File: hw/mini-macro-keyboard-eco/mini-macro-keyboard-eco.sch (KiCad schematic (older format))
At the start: 32 parts, among them J0 USB, J1 DEBUG_SWD, SW1 SW_Cherry_MX_1.00u_PCB, SW2 SW_Cherry_MX_1.00u_PCB, SW3 SW_Cherry_MX_1.00u_PCB, SW5 LAYOUT, SW6 BACKLIGHT, U1 USBLC6-2SC6, U2 XC6206P322MR, U3 STM32F070F6P6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

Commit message: feat(hw): add rooting
Signed-off-by: Ivan Kovalenko <s1ckretbox@gmail.com>
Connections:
- net LED_1: now also U3.9 (PA3); no longer U3.6 (PA0)
- net LED_3: now also U3.6 (PA0); no longer U3.9 (PA3)
- net SW_1: now also U3.13 (PA7); no longer U3.11 (PA5)
- net SW_3: now also U3.11 (PA5); no longer U3.13 (PA7)
- net USB_CONN_D+: now also U1.3 (I/O2); no longer U1.1 (I/O1)
- net USB_CONN_D-: now also U1.1 (I/O1); no longer U1.3 (I/O2)
- net USB_D+: now also U1.4 (I/O2); no longer U1.6 (I/O1)
- net USB_D-: now also U1.6 (I/O1); no longer U1.4 (I/O2)
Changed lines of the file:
@@
 Text GLabel 4350 3000 2    50   Input ~ 0
 USB_D-
-Text GLabel 4350 2500 2    50   Input ~ 0
+Text GLabel 4350 2200 2    50   Input ~ 0
 LED_3
 Text GLabel 4350 2300 2    50   Input ~ 0
 LED_2
-Text GLabel 4350 2200 2    50   Input ~ 0
+Text GLabel 4350 2500 2    50   Input ~ 0
 LED_1
-Text GLabel 4350 2700 2    50   Input ~ 0
+Text GLabel 4350 2900 2    50   Input ~ 0
 SW_1
 Text GLabel 4350 2800 2    50   Input ~ 0
 SW_2
-Text GLabel 4350 2900 2    50   Input ~ 0
+Text GLabel 4350 2700 2    50   Input ~ 0
 SW_3
 Text GLabel 3050 3100 0    50   Input ~ 0
@@
 Text GLabel 1650 4950 2    50   Input ~ 0
 USB_CONN_D-
-Text GLabel 3200 4900 0    50   Input ~ 0
+Text GLabel 4000 4900 2    50   Input ~ 0
 USB_CONN_D+
 $Comp
@@
 	1    0    0    -1
 $EndComp
+Text GLabel 4000 4700 2    50   Input ~ 0
+USB_D+
+Text GLabel 3200 4900 0    50   Input ~ 0
+USB_CONN_D-
 Text GLabel 3200 4700 0    50   Input ~ 0
-USB_D+
-Text GLabel 4000 4900 2    50   Input ~ 0
-USB_CONN_D-
-Text GLabel 4000 4700 2    50   Input ~ 0
 USB_D-
 Text GLabel 7650 900  0    50   Input ~ 0

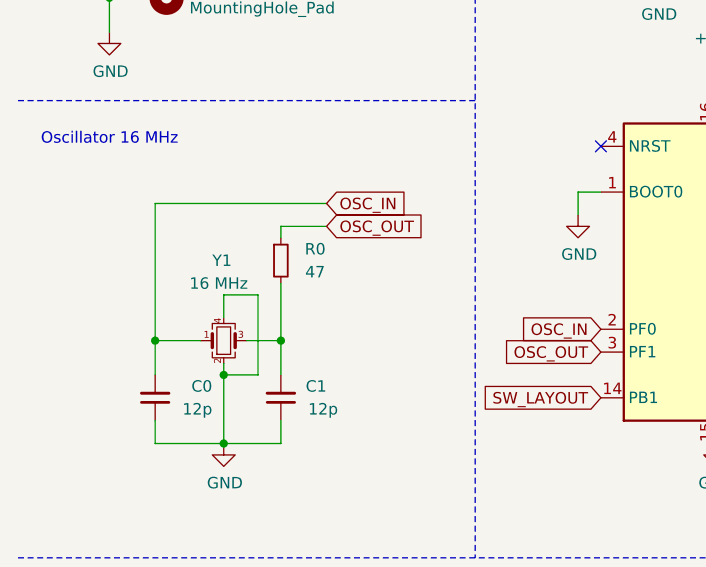
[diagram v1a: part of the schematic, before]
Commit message: fix(hw, #3): remove R0 resistor
Signed-off-by: Ivan Kovalenko <s1ckretbox@gmail.com>
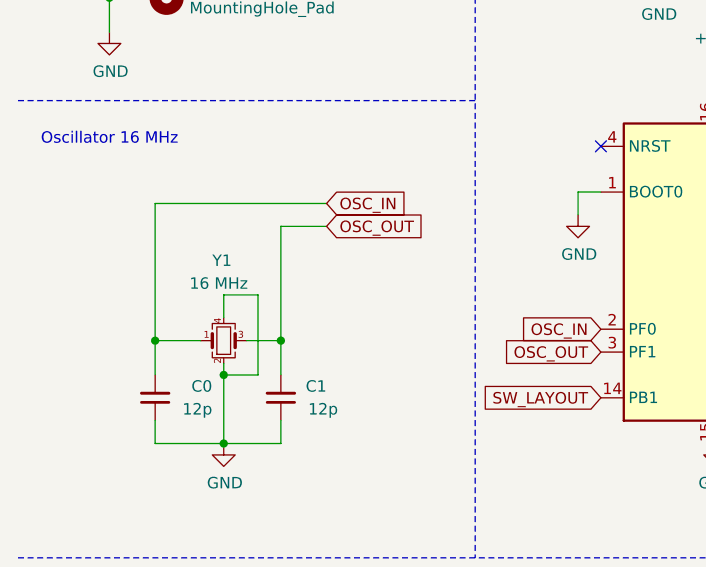
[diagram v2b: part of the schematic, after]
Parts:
- removed R0: 47, Resistor_SMD:R_0402_1005Metric, symbol mini-macro-keyboard-eco-rescue:R_Small-Device
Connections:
- net OSC_OUT: now also C1.2, Y1.3
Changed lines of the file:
@@
 	-1   0    0    1
-$EndComp
-$Comp
-L mini-macro-keyboard-eco-rescue:R_Small-Device R0
-U 1 1 60011E97
-P 1650 2700
-F 0 "R0" H 1800 2750 50  0000 C CNN
-F 1 "47" H 1800 2650 50  0000 C CNN
-F 2 "Resistor_SMD:R_0402_1005Metric" H 1650 2700 50  0001 C CNN
-F 3 "~" H 1650 2700 50  0001 C CNN
-	1    1650 2700
-	1    0    0    -1
 $EndComp
 Text GLabel 1850 2450 2    50   Input ~ 0
@@
 Wire Wire Line
 	1400 3200 1400 3500
-Wire Wire Line
-	1650 2800 1650 3050
 Connection ~ 1650 3050
 Connection ~ 1100 3050
 Wire Wire Line
 	1850 2550 1650 2550
-Wire Wire Line
-	1650 2550 1650 2600
 Wire Notes Line
 	7000 500  7000 2000
@@
 Wire Wire Line
 	900  1050 900  1300
+Wire Wire Line
+	1650 2550 1650 3050
 $EndSCHEMATC

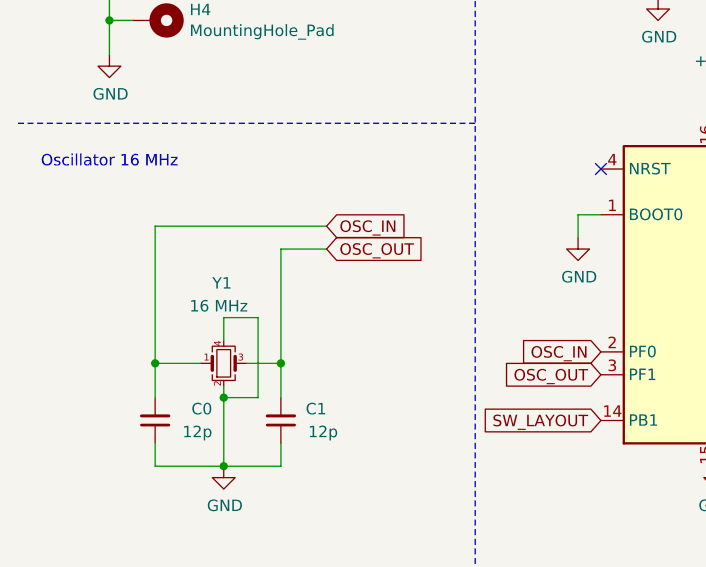
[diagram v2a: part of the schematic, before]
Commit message: feat(hw): add jlcpcb parts number
Signed-off-by: Ivan Kovalenko <s1ckretbox@gmail.com>
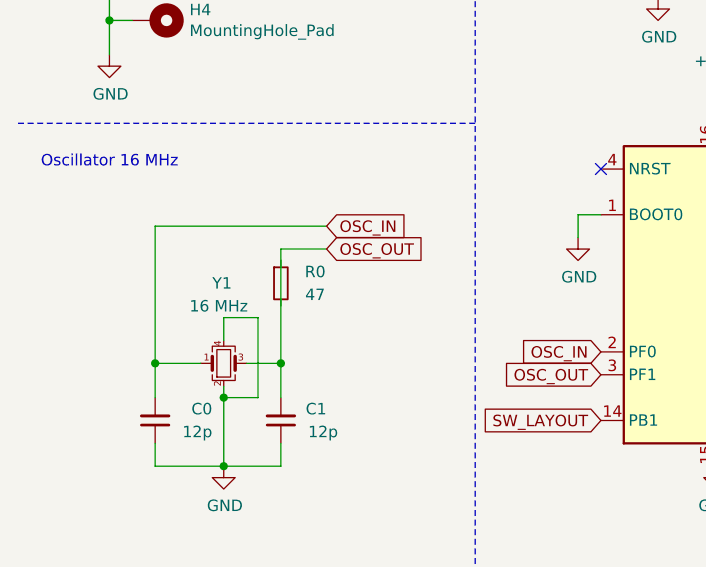
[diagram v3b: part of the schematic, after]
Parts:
- added R0: 47, Resistor_SMD:R_0402_1005Metric, symbol mini-macro-keyboard-eco-rescue:R_Small-Device
- C0, C1: LCSC Part # (none) -> C1547
- C2, C3, C7: LCSC Part # (none) -> C1525
- C4: LCSC Part # (none) -> C19666
- C5, C6: LCSC Part # (none) -> C52923
- D1, D2, D3: LCSC Part # (none) -> C72041
- R1, R2, R3: LCSC Part # (none) -> C23138
- R5, R6: LCSC Part # (none) -> C25744
- U1: LCSC Part # (none) -> C7519
- U2: LCSC Part # (none) -> C5446
- U3: LCSC Part # (none) -> C86951
- Y1: LCSC Part # (none) -> C13738
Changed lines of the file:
@@
 F 2 "Capacitor_SMD:C_0402_1005Metric" H 3300 1200 50  0001 C CNN
 F 3 "~" H 3300 1200 50  0001 C CNN
+F 4 "C1525" H 3300 1200 50  0001 C CNN "LCSC Part #"
 	1    3300 1200
 	1    0    0    -1
@@
 F 2 "Capacitor_SMD:C_0402_1005Metric" H 3600 1200 50  0001 C CNN
 F 3 "~" H 3600 1200 50  0001 C CNN
+F 4 "C1525" H 3600 1200 50  0001 C CNN "LCSC Part #"
 	1    3600 1200
 	1    0    0    -1
@@
 F 2 "Capacitor_SMD:C_0402_1005Metric" H 3950 1200 50  0001 C CNN
 F 3 "~" H 3950 1200 50  0001 C CNN
+F 4 "C19666" H 3950 1200 50  0001 C CNN "LCSC Part #"
 	1    3950 1200
 	1    0    0    -1
@@
 F 2 "Capacitor_SMD:C_0402_1005Metric" H 1100 3300 50  0001 C CNN
 F 3 "~" H 1100 3300 50  0001 C CNN
+F 4 "C1547" H 1100 3300 50  0001 C CNN "LCSC Part #"
 	1    1100 3300
 	-1   0    0    1
+$EndComp
+$Comp
+L mini-macro-keyboard-eco-rescue:R_Small-Device R0
+U 1 1 60011E97
+P 1650 2700
+F 0 "R0" H 1800 2750 50  0000 C CNN
+F 1 "47" H 1800 2650 50  0000 C CNN
+F 2 "Resistor_SMD:R_0402_1005Metric" H 1650 2700 50  0001 C CNN
+F 3 "~" H 1650 2700 50  0001 C CNN
+F 4 "C25792" H 1650 2700 50  0001 C CNN "LCSC Part #"
+	1    1650 2700
+	1    0    0    -1
 $EndComp
 Text GLabel 1850 2450 2    50   Input ~ 0
@@
 F 2 "Package_TO_SOT_SMD:SOT-23-6" H 3600 4300 50  0001 C CNN
 F 3 "https://www.st.com/resource/en/datasheet/usblc6-2.pdf" H 3800 5150 50  0001 C CNN
+F 4 "C7519" H 3600 4800 50  0001 C CNN "LCSC Part #"
 	1    3600 4800
 	1    0    0    -1
@@
 F 2 "LED_SMD:LED_0603_1608Metric" V 7900 900 50  0001 C CNN
 F 3 "~" V 7900 900 50  0001 C CNN
+F 4 "C72041" H 7900 900 50  0001 C CNN "LCSC Part #"
 	1    7900 900
 	-1   0    0    1
@@
 F 2 "Resistor_SMD:R_0603_1608Metric" H 8250 900 50  0001 C CNN
 F 3 "~" H 8250 900 50  0001 C CNN
+F 4 "C23138" H 8250 900 50  0001 C CNN "LCSC Part #"
 	1    8250 900
 	0    -1   -1   0
@@
 F 2 "LED_SMD:LED_0603_1608Metric" V 7900 1250 50  0001 C CNN
 F 3 "~" V 7900 1250 50  0001 C CNN
+F 4 "C72041" H 7900 1250 50  0001 C CNN "LCSC Part #"
 	1    7900 1250
 	-1   0    0    1
@@
 F 2 "Resistor_SMD:R_0603_1608Metric" H 8250 1250 50  0001 C CNN
 F 3 "~" H 8250 1250 50  0001 C CNN
+F 4 "C23138" H 8250 1250 50  0001 C CNN "LCSC Part #"
 	1    8250 1250
 	0    -1   -1   0
@@
 F 2 "LED_SMD:LED_0603_1608Metric" V 7900 1600 50  0001 C CNN
 F 3 "~" V 7900 1600 50  0001 C CNN
+F 4 "C72041" H 7900 1600 50  0001 C CNN "LCSC Part #"
 	1    7900 1600
 	-1   0    0    1
@@
 F 2 "Resistor_SMD:R_0603_1608Metric" H 8250 1600 50  0001 C CNN
 F 3 "~" H 8250 1600 50  0001 C CNN
+F 4 "C23138" H 8250 1600 50  0001 C CNN "LCSC Part #"
 	1    8250 1600
 	0    -1   -1   0
@@
 F 2 "Capacitor_SMD:C_0402_1005Metric" H 9700 1200 50  0001 C CNN
 F 3 "~" H 9700 1200 50  0001 C CNN
+F 4 "C1525" H 9700 1200 50  0001 C CNN "LCSC Part #"
 	1    9700 1200
 	1    0    0    -1
@@
 F 2 "Package_TO_SOT_SMD:SOT-23" H 5850 1425 50  0001 C CIN
 F 3 "https://www.torexsemi.com/file/xc6206/XC6206.pdf" H 5850 1200 50  0001 C CNN
+F 4 "C5446" H 5850 1200 50  0001 C CNN "LCSC Part #"
 	1    5850 1200
 	1    0    0    -1
@@
 F 2 "Capacitor_SMD:C_0402_1005Metric" H 5400 1400 50  0001 C CNN
 F 3 "~" H 5400 1400 50  0001 C CNN
+F 4 "C52923" H 5400 1400 50  0001 C CNN "LCSC Part #"
 	1    5400 1400
 	1    0    0    -1
@@
 F 2 "Capacitor_SMD:C_0402_1005Metric" H 6300 1400 50  0001 C CNN
 F 3 "~" H 6300 1400 50  0001 C CNN
+F 4 "C52923" H 6300 1400 50  0001 C CNN "LCSC Part #"
 	1    6300 1400
 	1    0    0    -1
@@
 F 2 "Package_SO:TSSOP-20_4.4x6.5mm_P0.65mm" H 3150 2000 50  0001 R CNN
 F 3 "http://www.st.com/st-web-ui/static/active/en/resource/technical/document/datasheet/DM00141386.pdf" H 3750 2700 50  0001 C CNN
+F 4 "C86951" H 3750 2700 50  0001 C CNN "LCSC Part #"
 	1    3750 2700
 	1    0    0    -1
@@
 F 2 "Crystal:Crystal_SMD_3225-4Pin_3.2x2.5mm" H 1400 3050 50  0001 C CNN
 F 3 "~" H 1400 3050 50  0001 C CNN
+F 4 "C13738" H 1400 3050 50  0001 C CNN "LCSC Part #"
 	1    1400 3050
 	1    0    0    -1
@@
 F 2 "Capacitor_SMD:C_0402_1005Metric" H 1650 3300 50  0001 C CNN
 F 3 "~" H 1650 3300 50  0001 C CNN
+F 4 "C1547" H 1650 3300 50  0001 C CNN "LCSC Part #"
 	1    1650 3300
 	-1   0    0    1
@@
 F 2 "Resistor_SMD:R_0402_1005Metric" H 9950 3400 50  0001 C CNN
 F 3 "~" H 9950 3400 50  0001 C CNN
+F 4 "C25744" H 9950 3400 50  0001 C CNN "LCSC Part #"
 	1    9950 3400
 	0    -1   -1   0
@@
 F 2 "Resistor_SMD:R_0402_1005Metric" H 9950 2650 50  0001 C CNN
 F 3 "~" H 9950 2650 50  0001 C CNN
+F 4 "C25744" H 9950 2650 50  0001 C CNN "LCSC Part #"
 	1    9950 2650
 	0    -1   -1   0
